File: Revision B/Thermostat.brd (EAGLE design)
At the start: 50.8 x 50.8 mm, 26 parts, among them T1 MOSFET, T2 MOSFET, T3 MOSFET

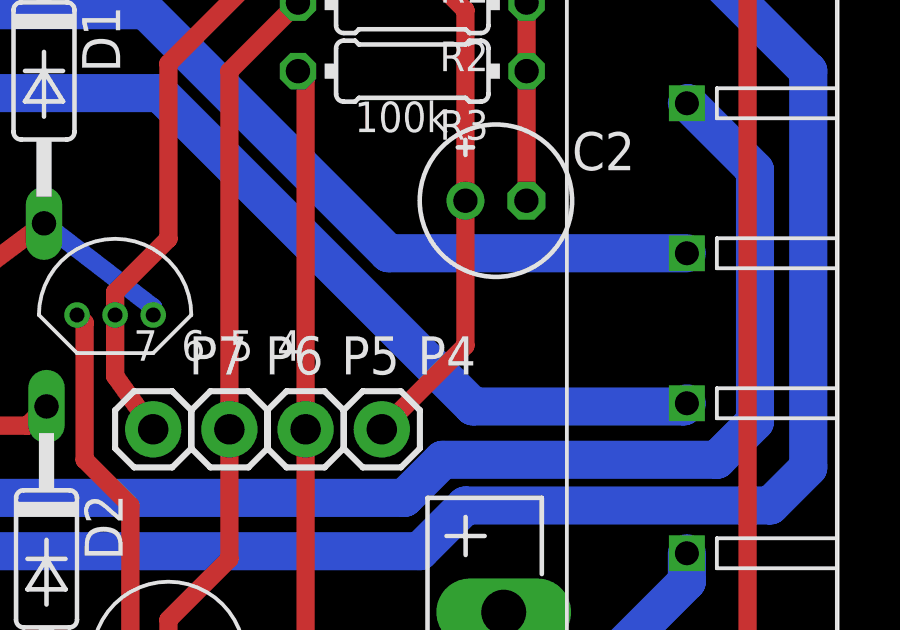
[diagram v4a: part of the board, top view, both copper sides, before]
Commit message: Added Temperature Sensor Resistor
Added a 150k resistor to the temperature sensor to drop the amps to 5uA,
below the 7uA output of the temperature sensor, in order to allow the
capacitor to charge.
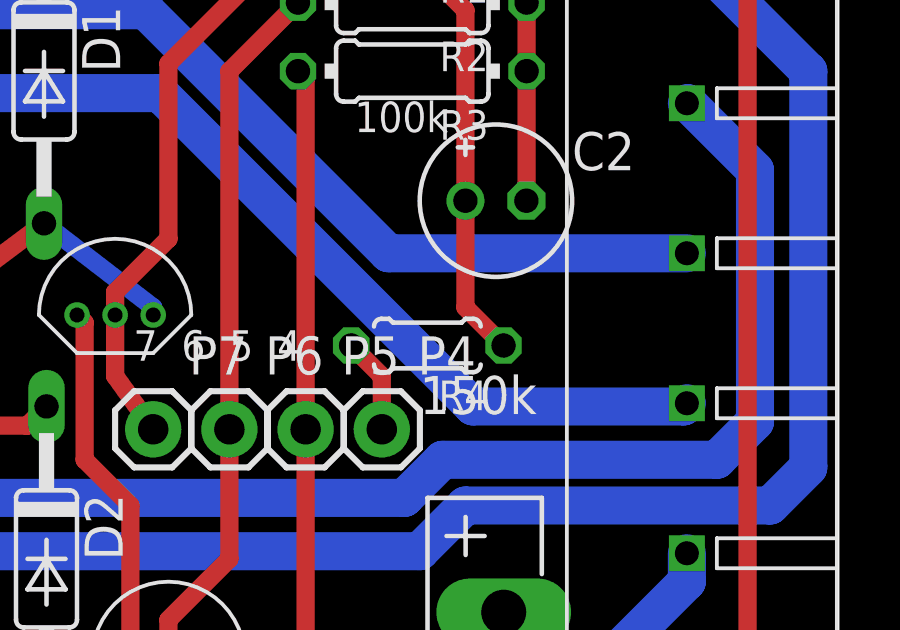
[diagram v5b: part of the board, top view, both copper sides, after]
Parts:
- added R4: (no value), rcl:0204/5
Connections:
- new net N$5: P4.1, R4.2
- net N$4: now also R4.1; no longer P4.1
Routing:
- net N$4: track 30.0 -> 26.6 mm
- net N$5: track 0.00 -> 3.22 mm
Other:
- board text added: "150k"
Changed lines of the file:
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@@
 <text x="13.3223" y="6.096" size="2.54" layer="121" font="vector" rot="R90">Rev. B</text>
 <text x="10.7823" y="6.096" size="2.54" layer="122" font="vector" rot="MR90">Android Thermostat</text>
+<text x="36.83" y="31.75" size="1.27" layer="121">150k</text>
 </plain>
 <attributes>
@@
 <element name="T1" library="android-thermostat" package="TRANSISTOR" value="MOSFET" x="26.6763" y="35.052" rot="R90"/>
 <element name="C2" library="rcl" package="E2-5" value="" x="39.37" y="38.862"/>
+<element name="R4" library="rcl" package="0204/5" value="" x="37.084" y="34.036" rot="R180"/>
 </elements>
 <signals>
@@
 <contactref element="U$1" pad="DATA-2"/>
 <contactref element="C2" pad="+"/>
-<contactref element="P4" pad="1"/>
 <wire x1="27.6923" y1="48.26" x2="27.6923" y2="47.4917" width="0.6096" layer="1"/>
 <wire x1="27.6923" y1="47.4917" x2="28.956" y2="46.228" width="0.6096" layer="1"/>
@@
 <wire x1="34.29" y1="49.276" x2="38.354" y2="45.212" width="0.6096" layer="1"/>
 <wire x1="38.354" y1="45.212" x2="38.354" y2="38.862" width="0.6096" layer="1"/>
-<wire x1="38.354" y1="38.862" x2="38.354" y2="34.0297" width="0.6096" layer="1"/>
-<wire x1="38.354" y1="34.0297" x2="35.5663" y2="31.242" width="0.6096" layer="1"/>
+<contactref element="R4" pad="1"/>
+<wire x1="38.354" y1="38.862" x2="38.354" y2="35.306" width="0.6096" layer="1"/>
+<wire x1="38.354" y1="35.306" x2="39.624" y2="34.036" width="0.6096" layer="1"/>
+</signal>
+<signal name="N$5">
+<contactref element="R4" pad="2"/>
+<contactref element="P4" pad="1"/>
+<wire x1="35.5663" y1="31.242" x2="35.5663" y2="33.0137" width="0.6096" layer="1"/>
+<wire x1="35.5663" y1="33.0137" x2="34.544" y2="34.036" width="0.6096" layer="1"/>
 </signal>
 </signals>

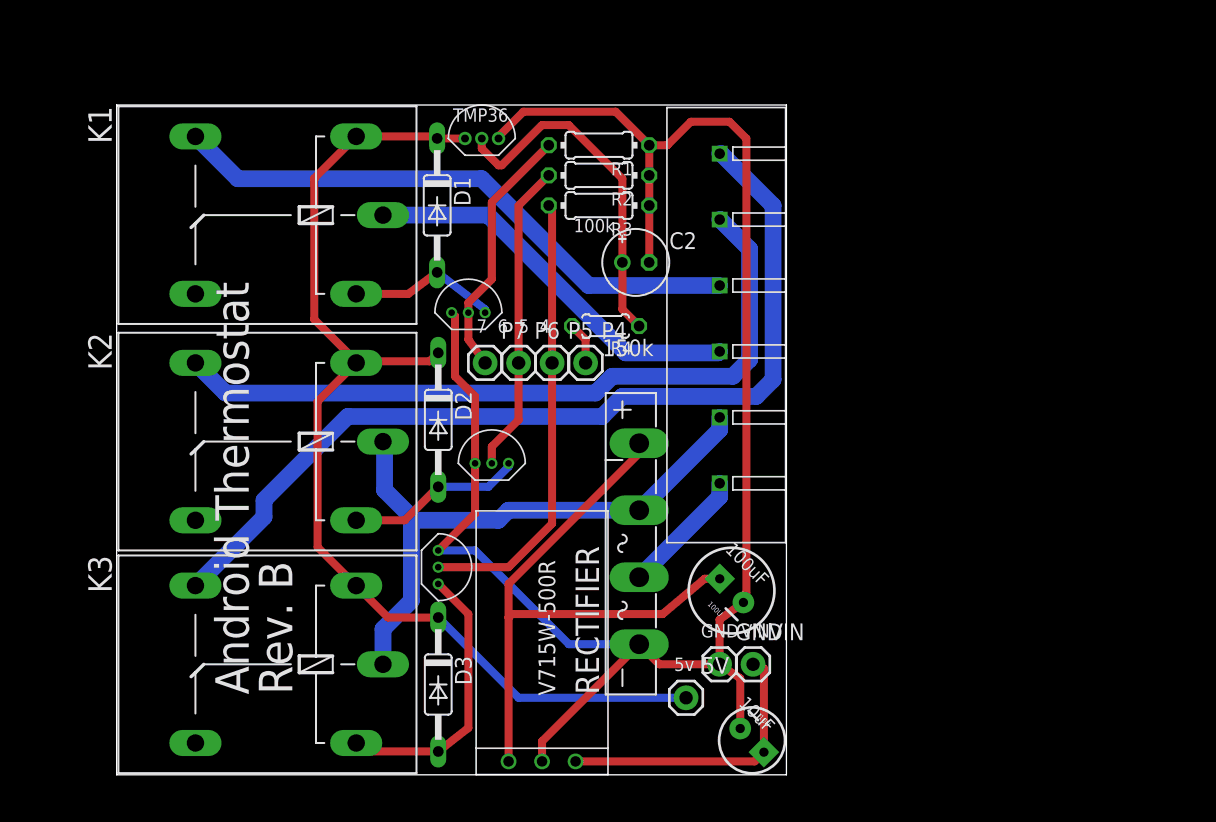
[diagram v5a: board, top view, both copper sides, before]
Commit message: Made tweeks after first print
Moved relay bodies off the board to provide more space.
Widened holes for temp sensor, transistors, capacitor and terminal
Spread out components that were overlapping.
Removed wires crossing low-pass filter.
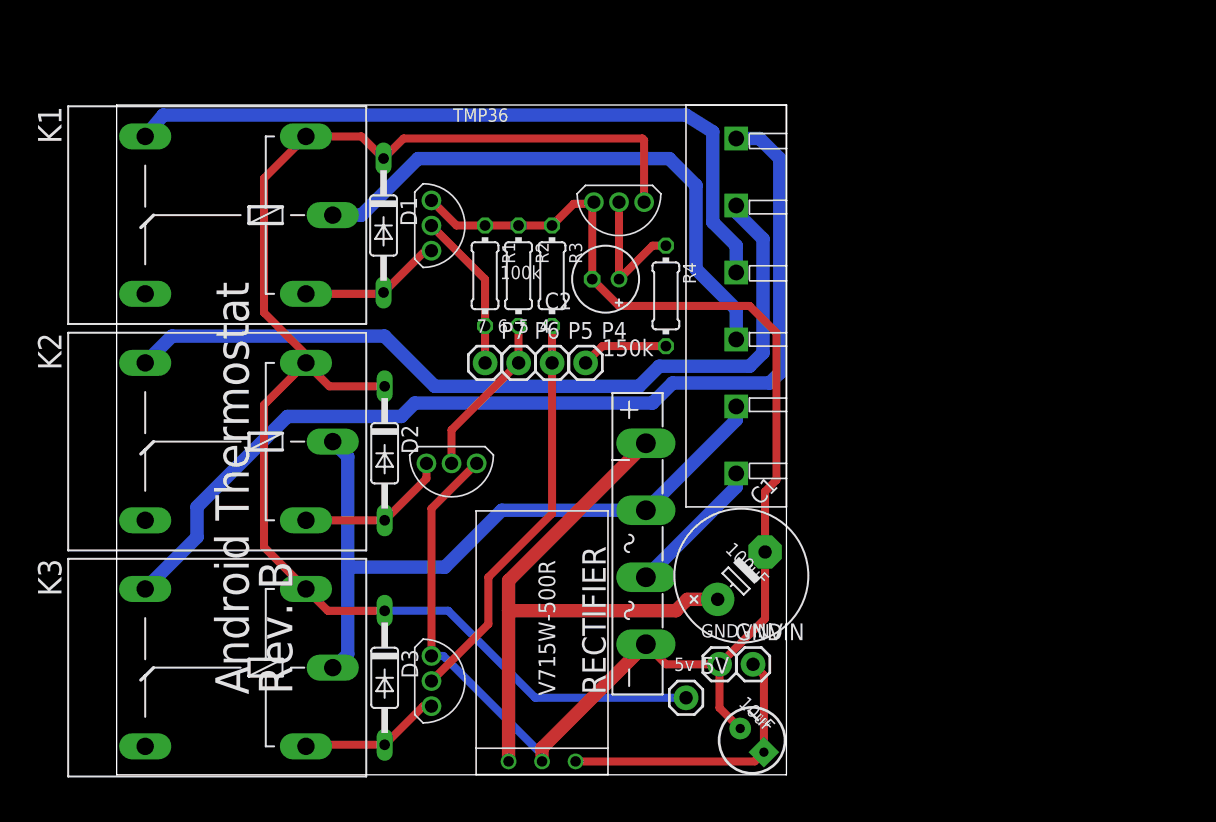
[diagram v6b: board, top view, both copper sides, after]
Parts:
- removed 100U: (no value), SparkFun-Passives:CPOL-RADIAL-100UF-25V
- removed T1, T2, T3: MOSFET, android-thermostat:TRANSISTOR
- added C1: (no value), rcl:E5-10,5
- added U$4, U$5, U$6: TRANSISTOR, android-thermostat:TRANSISTOR
- R4: device rcl:0204/5 -> rcl:0204/7
- moved R1 13.1 mm to (27.9, 37.9), turned to 270 degrees
- moved U$1 11.5 mm to (38.1, 43.4), turned to 270 degrees
- moved R2 9.76 mm to (30.5, 37.9), turned to 270 degrees
- moved R3 6.41 mm to (33.0, 37.9), turned to 270 degrees
- moved R4 5.11 mm to (41.7, 36.3), turned to 270 degrees
- moved D2 4.79 mm to (20.3, 24.4)
- moved D1 4.34 mm to (20.2, 41.7)
- moved D3 4.10 mm to (20.3, 7.36)
- moved K3 3.82 mm to (6.86, 8.13)
- moved K1 3.81 mm to (6.86, 42.4)
- moved K2 3.81 mm to (6.86, 25.3)
- moved C2 2.62 mm to (37.1, 37.6), turned to 180 degrees
- moved U$3 1.57 mm to (47.0, 35.6)
- moved RECTIFIER 0.51 mm to (40.1, 17.5)
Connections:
- removed net N$16: 5V.1, U$1.VCC-1
- net +5V: now also 5V.1, U$1.VC1
- net GND: now also C1.-, U$1.GND3, U$4.S, U$5.S, U$6.S; no longer 100U.2, T1.S, T2.S, T3.S, U$1.GND-3
- net N$17: now also U$4.G; no longer T3.G
- net N$18: now also U$4.D; no longer T3.D
- net N$2: now also U$5.G; no longer T2.G
- net N$24: now also C1.+; no longer 100U.1
- net N$3: now also U$5.D; no longer T2.D
- net N$4: now also U$1.OUT2; no longer U$1.DATA-2
- net N$6: now also U$6.G; no longer T1.G
- net N$7: now also U$6.D; no longer T1.D
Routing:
- net +5V: track 59.0 -> 110.3 mm
- net N$16: track 23.4 -> 0.00 mm
- net GND: track 134.3 -> 113.6 mm
- net N$4: track 26.6 -> 10.6 mm
- net N$1: track 29.9 -> 43.1 mm
- net N$14: track 44.4 -> 55.6 mm
- net N$2: track 23.6 -> 12.5 mm
- net N$18: track 21.0 -> 10.8 mm
- net N$9: track 45.8 -> 53.3 mm
- net N$6: track 19.4 -> 12.1 mm
- net N$15: track 55.6 -> 62.3 mm
- net N$13: track 69.9 -> 76.4 mm
- net N$17: track 34.2 -> 30.7 mm
- net N$5: track 3.22 -> 6.62 mm
- net N$3: track 13.5 -> 11.6 mm
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
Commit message: Prepared for second print
Moved components to within spacing tolerances.
Added and moved labels.
Ordered second print.
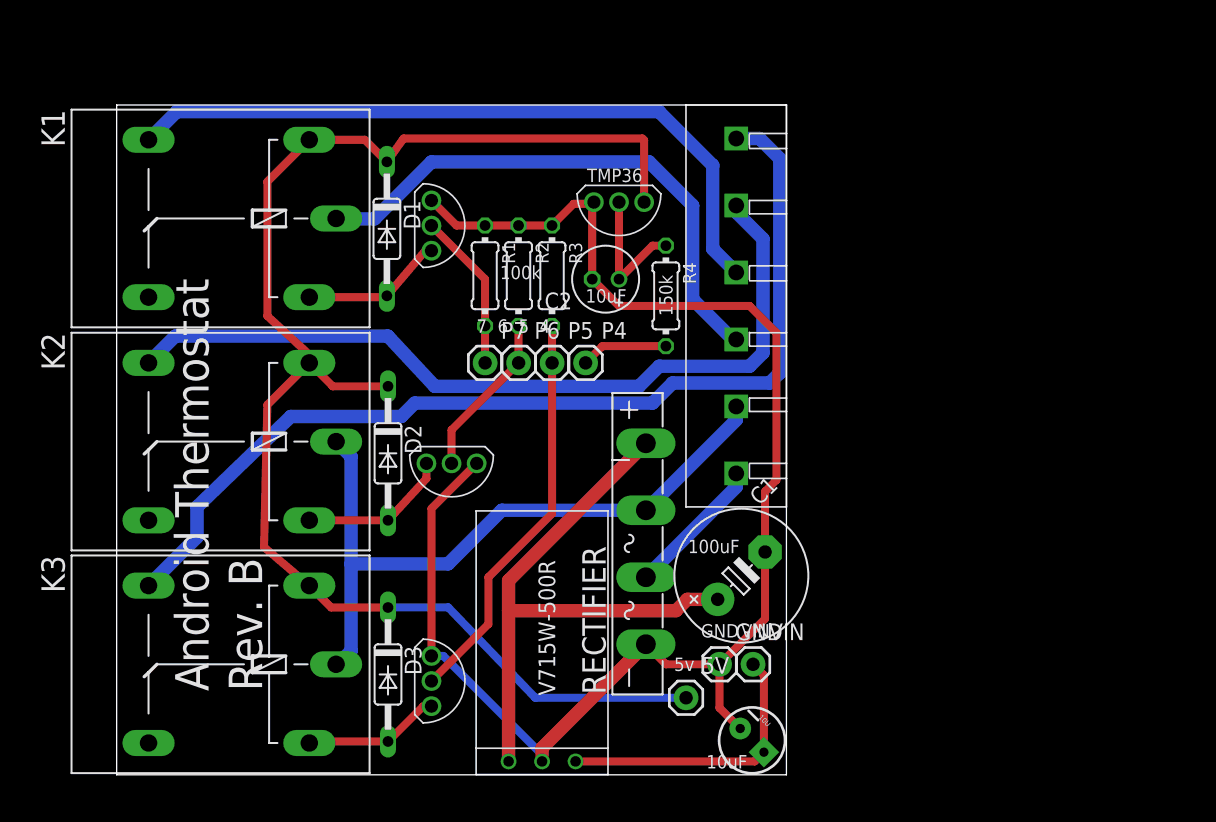
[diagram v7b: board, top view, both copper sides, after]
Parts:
- moved D3 0.36 mm to (20.6, 7.61)
- moved K3 0.36 mm to (7.12, 8.38)
- moved K1 0.36 mm to (7.12, 42.2)
- moved D1 0.36 mm to (20.5, 41.4)
- moved D2 0.25 mm to (20.6, 24.4)
- moved K2 0.25 mm to (7.12, 25.3)
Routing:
- net N$14: track 55.6 -> 54.2 mm
- net N$1: track 43.1 -> 41.9 mm
- net N$9: track 53.3 -> 52.7 mm

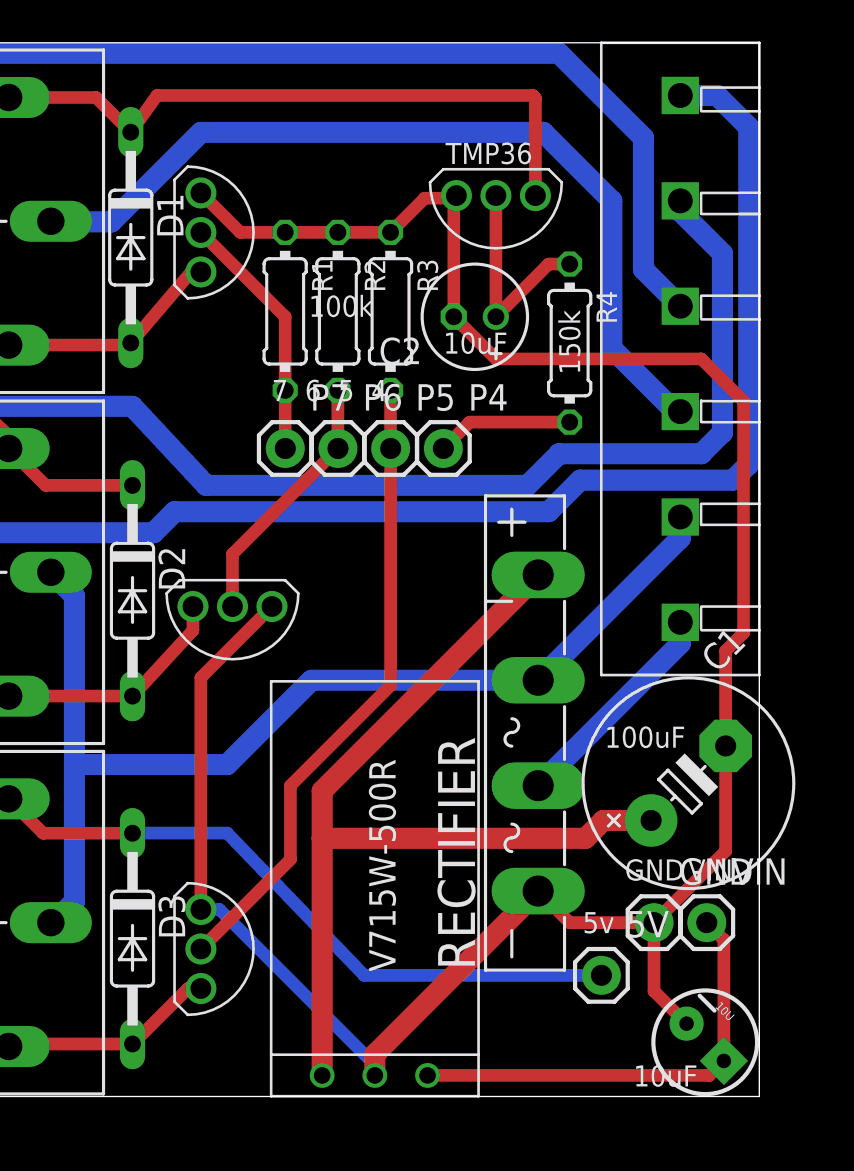
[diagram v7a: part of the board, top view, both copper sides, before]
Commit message: Moved Temperature Pin
Moved the temperature sensor input from PIN 4 (digital) to PIN 43
(analog).  This required moving a number of components around on the
board.
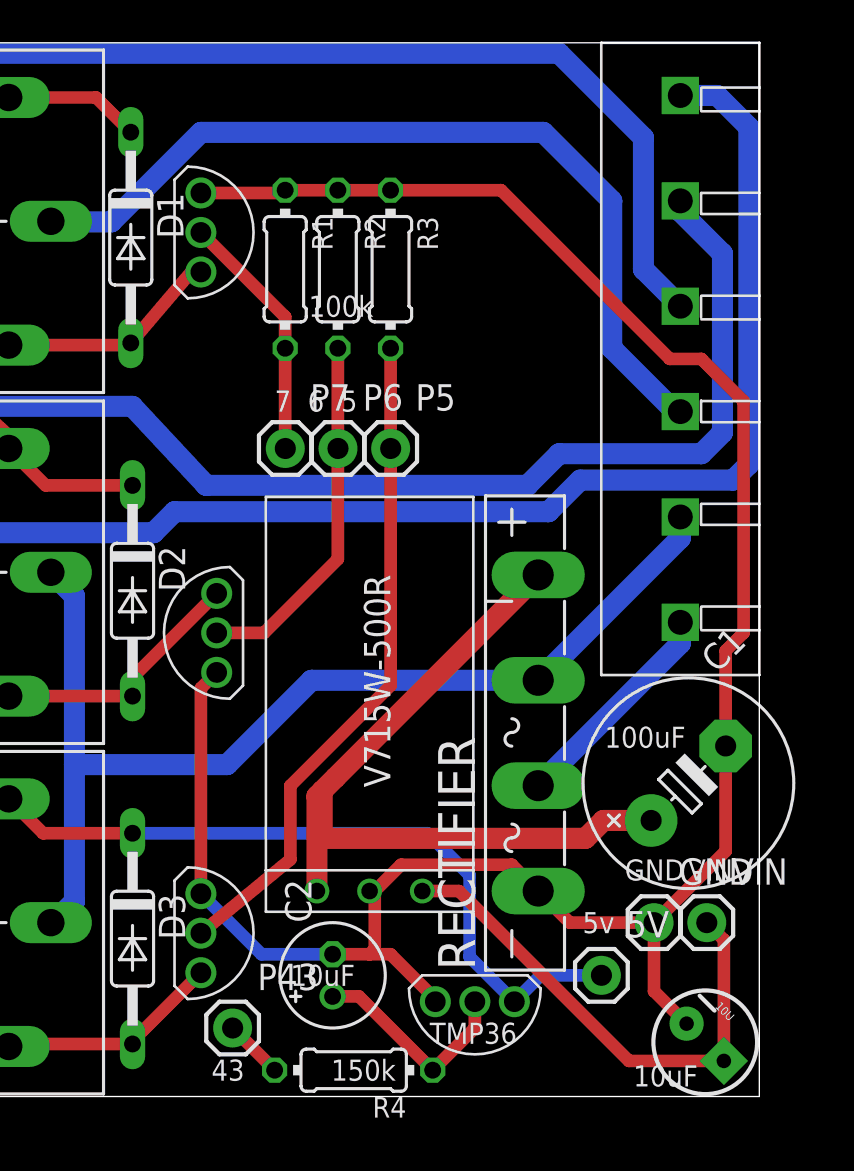
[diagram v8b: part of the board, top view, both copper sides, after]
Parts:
- removed P4: (no value), SparkFun-Connectors:1X01
- added P43: (no value), SparkFun-Connectors:1X01
- moved U$1 38.9 mm to (37.1, 4.57)
- moved R4 36.6 mm to (31.2, 1.27), turned to 180 degrees
- moved C2 32.5 mm to (30.2, 5.84), turned to 90 degrees
- moved U$2 8.89 mm to (32.0, 9.91)
- moved R1 2.03 mm to (27.9, 39.9)
- moved R2 2.03 mm to (30.5, 39.9)
- moved R3 2.03 mm to (33.0, 39.9)
- moved U$5 1.48 mm to (24.6, 22.4), turned to 180 degrees
- moved U$4 0.76 mm to (23.9, 7.87)
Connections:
- net N$5: now also P43.1; no longer P4.1
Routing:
- net +5V: track 110.1 -> 88.2 mm
- net GND: track 113.6 -> 106.0 mm
- net N$24: track 44.7 -> 38.2 mm
- net N$2: track 12.5 -> 17.5 mm
- net N$5: track 6.62 -> 2.87 mm
- net N$10: track 21.6 -> 24.9 mm
- net N$17: track 30.7 -> 32.2 mm
- net N$3: track 11.4 -> 12.6 mm
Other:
- board text added: "43"
- board text added: "7 6 5"
- board text removed: "7 6 5 4"
